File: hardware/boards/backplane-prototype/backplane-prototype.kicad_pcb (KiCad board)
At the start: 4 copper layers, 151.8 x 30.8 mm, 90 parts, among them J1 SLOT_1, J10 TC2030-IDC-NL SWD, J11 12V 3-WIRE FAN, J12 DS18B20 EXT SUPPLY, J2 XY308-2.54-3P / EXTERNAL CAN, J3 SLOT_2, J4 SLOT_3, J5 DC INPUT (GND / +VIN), J6 SLOT_4, J7 SLOT_5, J8 SLOT_6, J9 12V 3-WIRE FAN, Q1 AO3407A, Q2 2N7002, Q3 AO3407A, Q4 2N7002, U1 STM32C092GCU6, U2 LM5164DDAR, U3 LM5164DDAR, U4 INA237AIDGSR, U5 TCAN3413DR

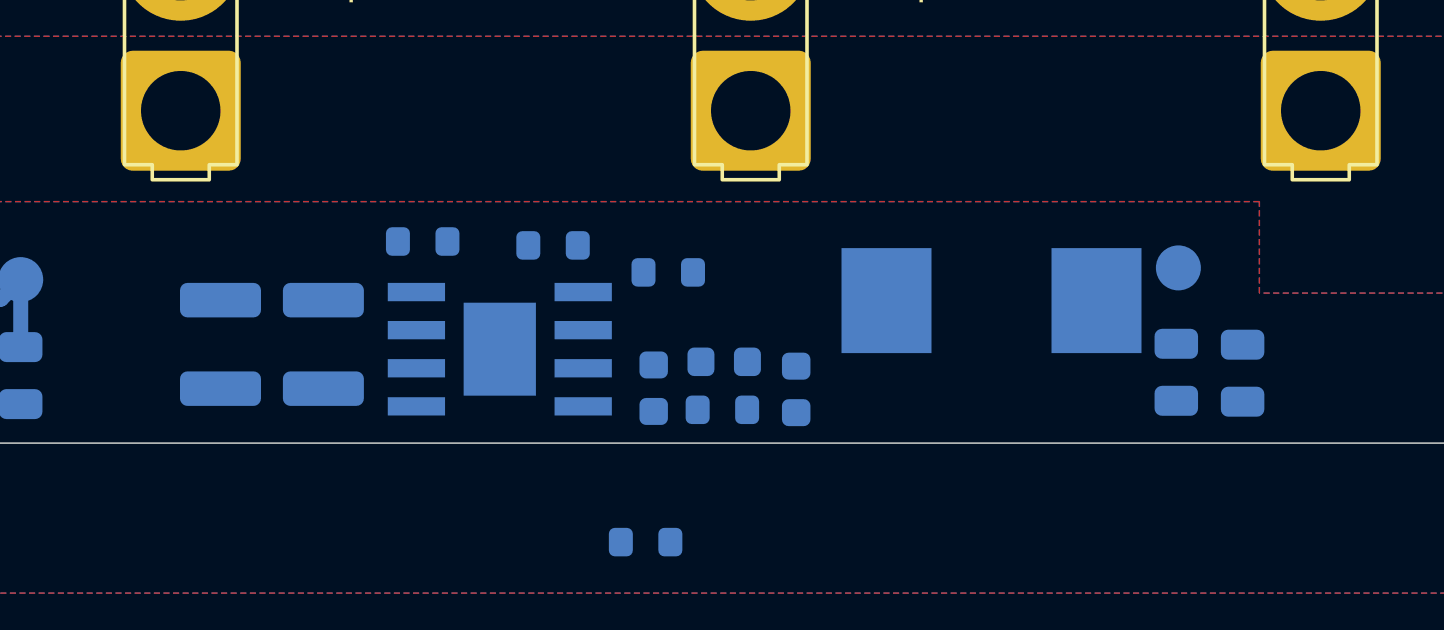
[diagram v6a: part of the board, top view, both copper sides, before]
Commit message: hardware: mirror 3v3 buck placement into 12v stage
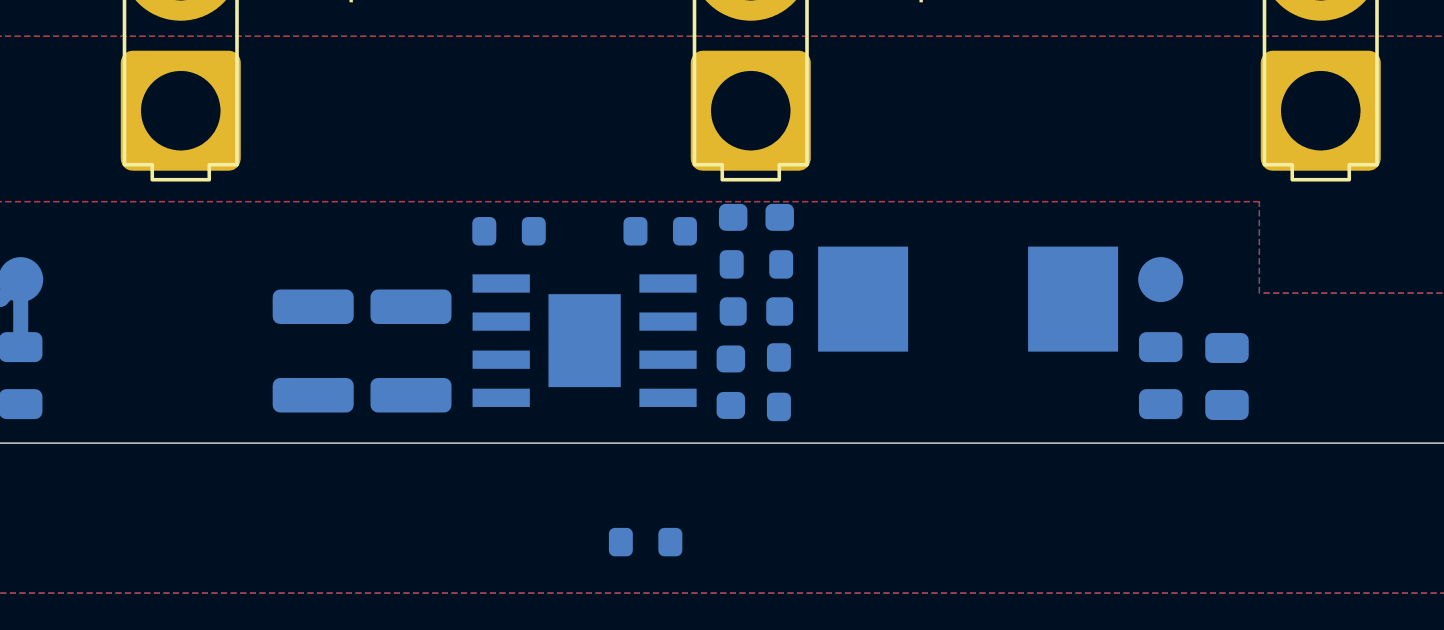
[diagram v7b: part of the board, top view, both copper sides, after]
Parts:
- moved C12 5.89 mm to (107.0, 70.0), turned to 0 degrees
- moved R8 3.60 mm to (103.8, 70.4)
- moved C7 3.10 mm to (92.2, 74.4)
- moved R7 2.95 mm to (107.0, 71.5)
- moved C8 2.93 mm to (95.5, 74.4)
- moved R6 2.90 mm to (98.7, 70.4)
- moved U3 2.84 mm to (101.3, 74.1)
- moved C9 2.58 mm to (106.1, 75.5)
- moved R9 2.10 mm to (107.7, 75.5), turned to 90 degrees
- moved C13 1.99 mm to (107.0, 73.1)
- moved L2 0.78 mm to (114.0, 72.7)
- moved TP4 0.71 mm to (120.5, 72.0), turned to 0 degrees
- moved C10 0.53 mm to (120.5, 75.2)
- moved C11 0.53 mm to (122.7, 75.3)
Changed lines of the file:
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@@
 	(footprint "mini-rack-power:L_PRODTech_PSPMAA0805"
 		(layer "B.Cu")
-		(at 114.82 72.75)
+		(at 114.04 72.7)
 		(descr "PROD Tech PSPMAA0805 power inductor, 8.0 x 8.5 mm, LCSC C2962892")
 		(tags "inductor power SMD 8x8.5 PSPMAA0805 C2962892")
@@
 	(footprint "Capacitor_SMD:C_1210_3225Metric"
 		(layer "B.Cu")
-		(at 89.12 74.21 -90)
+		(at 92.21 74.43 -90)
 		(descr "Capacitor SMD 1210 (3225 Metric), square (rectangular) end terminal, IPC-7351 nominal, (Body size source: IPC-SM-782 page 76, https://www.pcb-3d.com/wordpress/wp-content/uploads/ipc-sm-782a_amendment_1_and_2.pdf)")
 		(tags "capacitor")
@@
 	(footprint "Resistor_SMD:R_0603_1608Metric"
 		(layer "B.Cu")
-		(at 104.045 71.81 180)
+		(at 106.985 71.544167 180)
 		(descr "Resistor SMD 0603 (1608 Metric), square (rectangular) end terminal, IPC-7351 nominal, (Body size source: IPC-SM-782 page 72, https://www.pcb-3d.com/wordpress/wp-content/uploads/ipc-sm-782a_amendment_1_and_2.pdf)")
 		(tags "resistor")
@@
 	(footprint "Resistor_SMD:R_0603_1608Metric"
 		(layer "B.Cu")
-		(at 100.205 70.91 180)
+		(at 103.7775 70.44 180)
 		(descr "Resistor SMD 0603 (1608 Metric), square (rectangular) end terminal, IPC-7351 nominal, (Body size source: IPC-SM-782 page 72, https://www.pcb-3d.com/wordpress/wp-content/uploads/ipc-sm-782a_amendment_1_and_2.pdf)")
 		(tags "resistor")
@@
 	(footprint "Package_SO:TI_SO-PowerPAD-8"
 		(layer "B.Cu")
-		(at 98.43 74.37)
+		(at 101.2575 74.085)
 		(descr "8-Lead Plastic PSOP, Exposed Die Pad (TI DDA0008B, see http://www.ti.com/lit/ds/symlink/lm3404.pdf)")
 		(tags "SSOP 0.50 exposed pad")
@@
 	(footprint "Capacitor_SMD:C_0603_1608Metric"
 		(layer "B.Cu")
-		(at 103.56 75.67 -90)
+		(at 106.13125 75.47 -90)
 		(descr "Capacitor SMD 0603 (1608 Metric), square (rectangular) end terminal, IPC-7351 nominal, (Body size source: IPC-SM-782 page 76, https://www.pcb-3d.com/wordpress/wp-content/uploads/ipc-sm-782a_amendment_1_and_2.pdf)")
 		(tags "capacitor")
@@
 	(footprint "Resistor_SMD:R_0603_1608Metric"
 		(layer "B.Cu")
-		(at 95.86 70.78)
+		(at 98.7375 70.44)
 		(descr "Resistor SMD 0603 (1608 Metric), square (rectangular) end terminal, IPC-7351 nominal, (Body size source: IPC-SM-782 page 72, https://www.pcb-3d.com/wordpress/wp-content/uploads/ipc-sm-782a_amendment_1_and_2.pdf)")
 		(tags "resistor")
@@
 	(footprint "Resistor_SMD:R_0603_1608Metric"
 		(layer "B.Cu")
-		(at 105.85 76.39)
+		(at 107.735 75.47 90)
 		(descr "Resistor SMD 0603 (1608 Metric), square (rectangular) end terminal, IPC-7351 nominal, (Body size source: IPC-SM-782 page 72, https://www.pcb-3d.com/wordpress/wp-content/uploads/ipc-sm-782a_amendment_1_and_2.pdf)")
 		(tags "resistor")
@@
 	(footprint "Capacitor_SMD:C_0603_1608Metric"
 		(layer "B.Cu")
-		(at 105.91 74.79 180)
+		(at 106.985 73.113333 180)
 		(descr "Capacitor SMD 0603 (1608 Metric), square (rectangular) end terminal, IPC-7351 nominal, (Body size source: IPC-SM-782 page 76, https://www.pcb-3d.com/wordpress/wp-content/uploads/ipc-sm-782a_amendment_1_and_2.pdf)")
 		(tags "capacitor")
@@
 	(footprint "Capacitor_SMD:C_0805_2012Metric"
 		(layer "B.Cu")
-		(at 123.19 75.17 -90)
+		(at 122.67 75.28 -90)
 		(descr "Capacitor SMD 0805 (2012 Metric), square (rectangular) end terminal, IPC-7351 nominal, (Body size source: IPC-SM-782 page 76, https://www.pcb-3d.com/wordpress/wp-content/uploads/ipc-sm-782a_amendment_1_and_2.pdf, https://docs.google.com/spreadsheets/d/1BsfQQcO9C6DZCsRaXUlFlo91Tg2WpOkGARC1WS5S8t0/edit?usp=sharing)")
 		(tags "capacitor")
@@
 	(footprint "Capacitor_SMD:C_0603_1608Metric"
 		(layer "B.Cu")
-		(at 108.31 75.71 -90)
+		(at 106.985 69.975)
 		(descr "Capacitor SMD 0603 (1608 Metric), square (rectangular) end terminal, IPC-7351 nominal, (Body size source: IPC-SM-782 page 76, https://www.pcb-3d.com/wordpress/wp-content/uploads/ipc-sm-782a_amendment_1_and_2.pdf)")
 		(tags "capacitor")
@@
 	(footprint "Capacitor_SMD:C_1210_3225Metric"
 		(layer "B.Cu")
-		(at 92.55 74.21 -90)
+		(at 95.47 74.43 -90)
 		(descr "Capacitor SMD 1210 (3225 Metric), square (rectangular) end terminal, IPC-7351 nominal, (Body size source: IPC-SM-782 page 76, https://www.pcb-3d.com/wordpress/wp-content/uploads/ipc-sm-782a_amendment_1_and_2.pdf)")
 		(tags "capacitor")
@@
 	(footprint "Capacitor_SMD:C_0805_2012Metric"
 		(layer "B.Cu")
-		(at 120.98 75.14 -90)
+		(at 120.46 75.25 -90)
 		(descr "Capacitor SMD 0805 (2012 Metric), square (rectangular) end terminal, IPC-7351 nominal, (Body size source: IPC-SM-782 page 76, https://www.pcb-3d.com/wordpress/wp-content/uploads/ipc-sm-782a_amendment_1_and_2.pdf, https://docs.google.com/spreadsheets/d/1BsfQQcO9C6DZCsRaXUlFlo91Tg2WpOkGARC1WS5S8t0/edit?usp=sharing)")
 		(tags "capacitor")
@@
 	(footprint "TestPoint:TestPoint_Pad_D1.5mm"
 		(layer "B.Cu")
-		(at 121.05 71.66 180)
+		(at 120.46 72.05)
 		(descr "SMD pad as test Point, diameter 1.5mm")
 		(tags "test point SMD pad")

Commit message: checkpoint: save backplane routing progress
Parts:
- added REF**: OSHW-Logo_11.4x12mm_SilkScreen, Symbol:OSHW-Logo_11.4x12mm_SilkScreen, B.Cu at (61.0, 24.2)
- moved R10 15.7 mm to (111.5, 67.4)
- moved J2 5.04 mm to (33.7, 53.9), turned to 90 degrees
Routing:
- net +12V: track 0.00 -> 71.2 mm, vias 0 -> 3
- net /CAN-FD and Six Slots/CAN_EXT_N: track 0.00 -> 5.43 mm
- net +3V3: track 227.0 -> 229.1 mm
- net CAN_TX: vias 0 -> 1
- net CAN_RX: vias 0 -> 1
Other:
- board text added: "PD-CARRIER M2v1.26.08.29"
